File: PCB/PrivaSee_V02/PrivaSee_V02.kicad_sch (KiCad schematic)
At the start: 22 parts, among them J2 Batt_Solder_Point, SW1 (Generic toggle state switch), U2 LM358, U3 254, U4 DFR0568, U5 LM358, U6 ESP32-C5-DevKitC-1

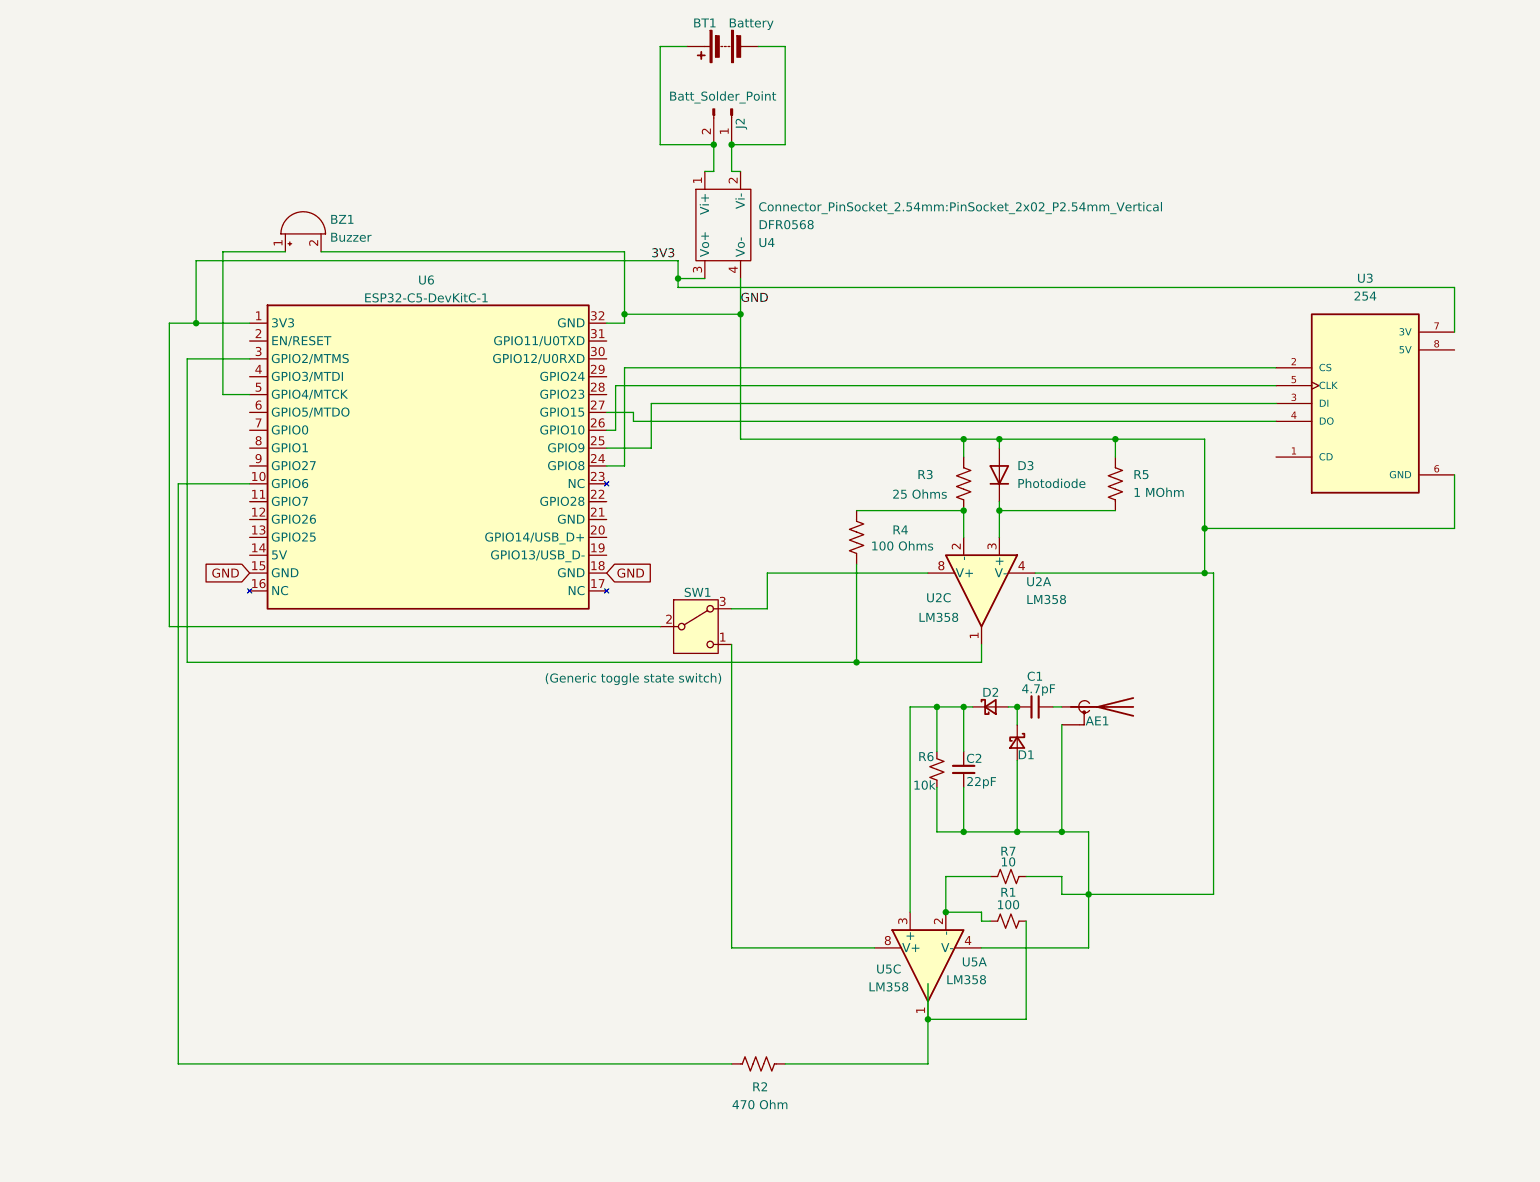
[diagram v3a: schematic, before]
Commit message: PCB Updates
Added a screen, updated the connector for the SMA through hole component, and rearranged to fit
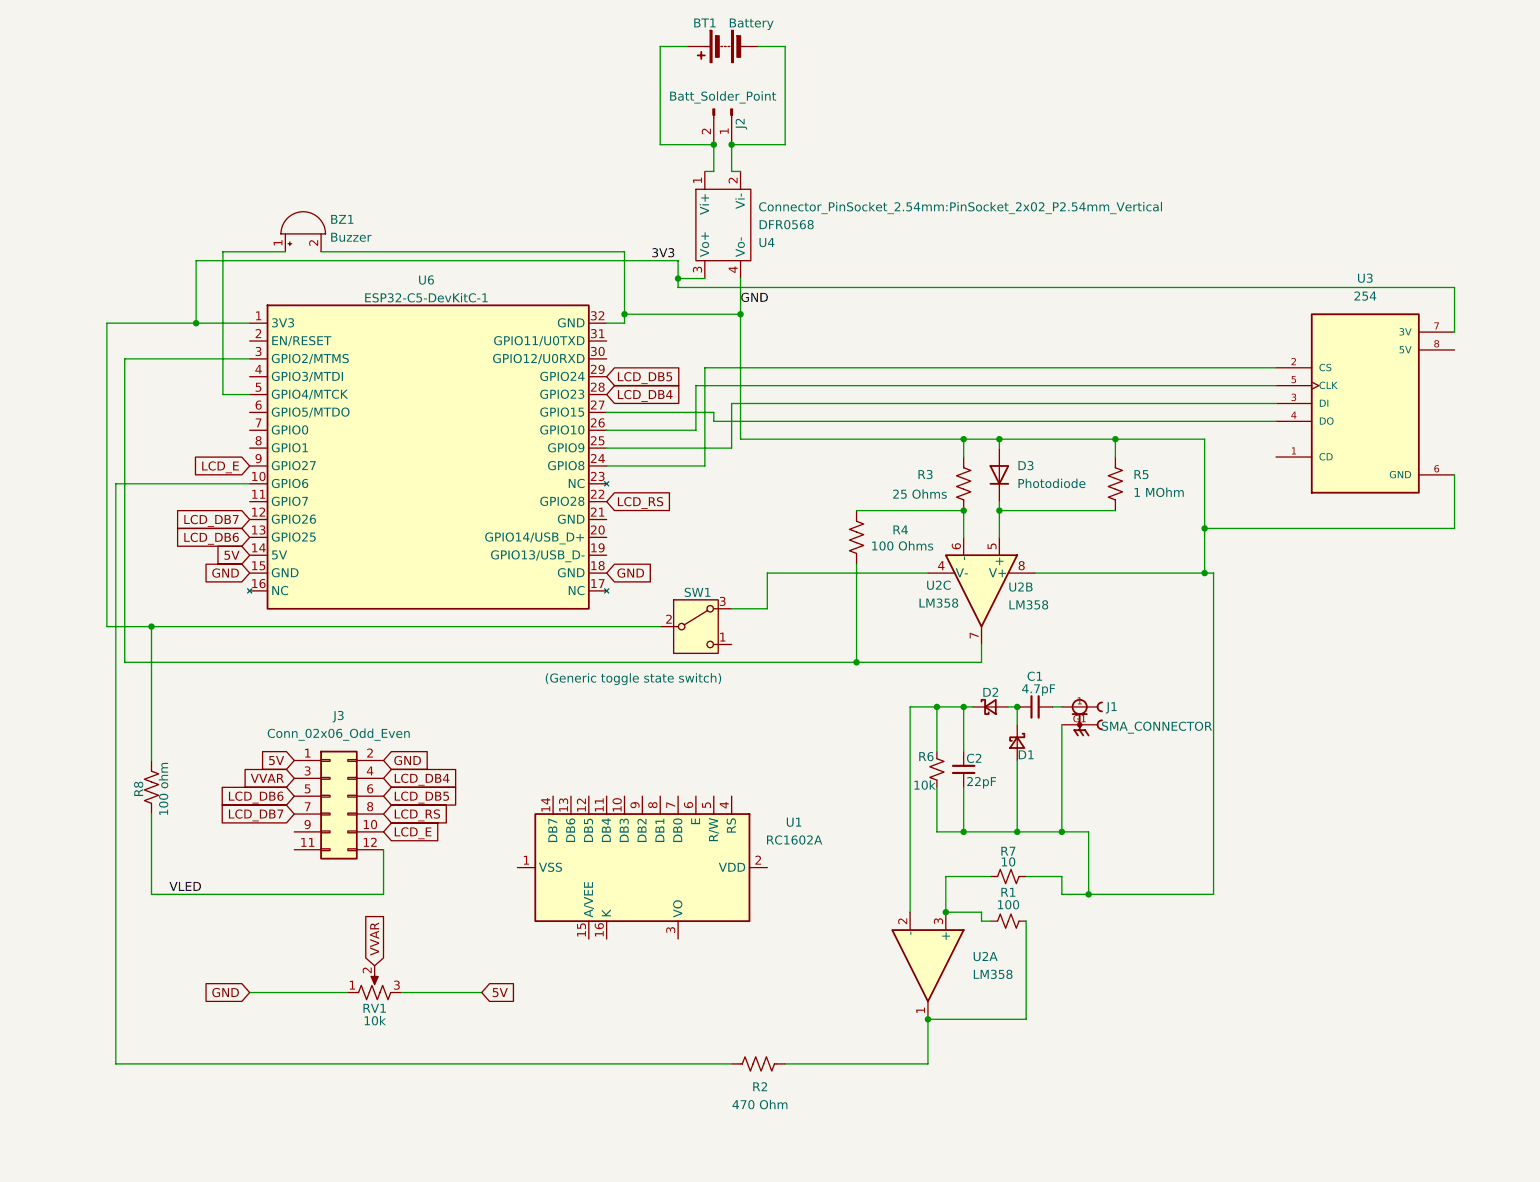
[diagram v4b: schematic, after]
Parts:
- removed AE1: SMA_Conn, RF_Antenna:Johanson_2450AT18x100_2400-2500Mhz, symbol Device:Antenna_Shield
- removed U5: LM358, Package_DIP:DIP-8_W7.62mm, symbol Amplifier_Operational:LM358
- added J1: SMA_CONNECTOR, SMA_CONNECTOR:LPRS_SMA_CONNECTOR, symbol SMA_CONNECTOR:SMA_CONNECTOR
- added J3: Conn_02x06_Odd_Even, Connector_PinHeader_2.54mm:PinHeader_2x06_P2.54mm_Vertical, symbol Connector_Generic:Conn_02x06_Odd_Even
- added R8: 100 ohm, Resistor_SMD:R_1206_3216Metric_Pad1.30x1.75mm_HandSolder, symbol Device:R_US
- added RV1: 10k, Potentiometer_THT:Potentiometer_ACP_CA6-H2,5_Horizontal, symbol Device:R_Potentiometer_US
- added U1: RC1602A, Display:RC1602A, symbol Display_Character:RC1602A
- added unit 2 of U2
- U2: footprint Package_DIP:DIP-8_W7.62mm -> Package_DIP:DIP-8_W7.62mm_Socket
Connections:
- net 3V3: now also R8.1
- net GND: now also U2.8 (V+), J1.G1, J1.G2, J1.G3, J1.G4, J3.2 (Pin_2), RV1.1; no longer U2.4 (V-)
- net at R4.2, U6.3 (GPIO2/MTMS): now also U2.7; no longer U2.1
- net at R3.2, R4.1: now also U2.6 (-); no longer U2.2 (-)
- net at D3.1 (K), R5.2: now also U2.5 (+); no longer U2.3 (+)
- net at R1.2, R2.2: now also U2.1
- net at R1.1, R7.1: now also U2.3 (+)
- net at C2.2, D2.1 (K), R6.1: now also U2.2 (-)
- net at C1.2: now also J1.1
- net LCD_DB7: now reaches U6.12 (GPIO26)
- net LCD_DB7: now also J3.7 (Pin_7)
- net LCD_DB6: now reaches U6.13 (GPIO25)
- net LCD_DB6: now also J3.5 (Pin_5)
- net 5V: now reaches U6.14 (5V)
- net 5V: now also J3.1 (Pin_1), RV1.3
- net LCD_RS: now reaches U6.22 (GPIO28)
- net LCD_RS: now also J3.8 (Pin_8)
- net LCD_DB4: now reaches U6.28 (GPIO23)
- net LCD_DB4: now also J3.4 (Pin_4)
- net LCD_DB5: now reaches U6.29 (GPIO24)
- net LCD_DB5: now also J3.6 (Pin_6)
- net LCD_E: now reaches U6.9 (GPIO27)
- net LCD_E: now also J3.10 (Pin_10)
- net at SW1.3 (A): now also U2.4 (V-); no longer U2.8 (V+)
- new net VLED: J3.12 (Pin_12), R8.2
- new net VVAR: J3.3 (Pin_3), RV1.2

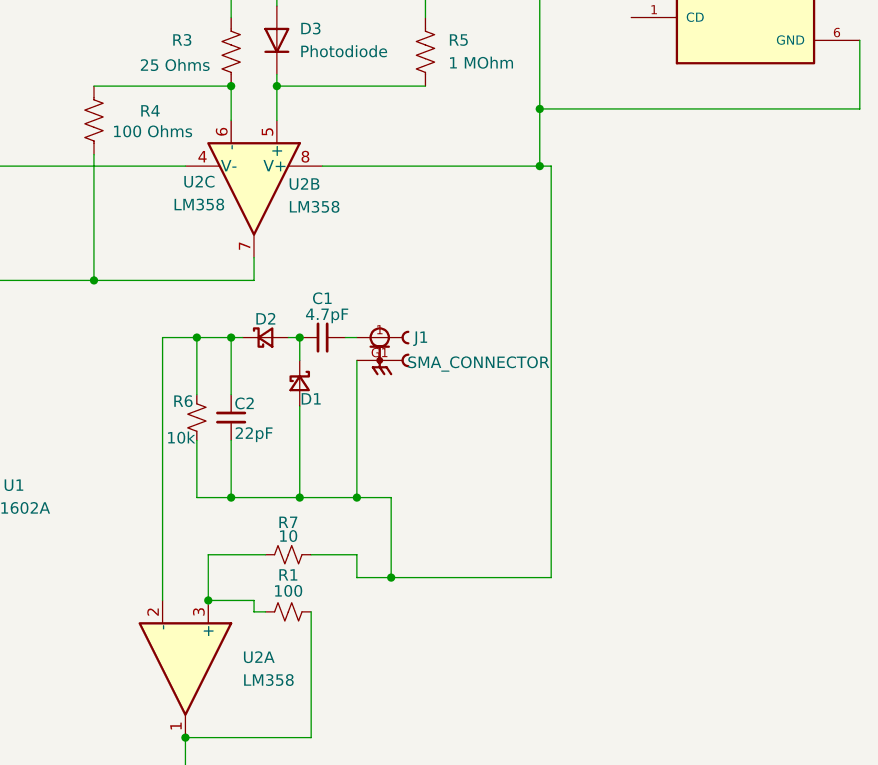
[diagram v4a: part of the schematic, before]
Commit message: RF parts placed
Swapped out the schematic with my components
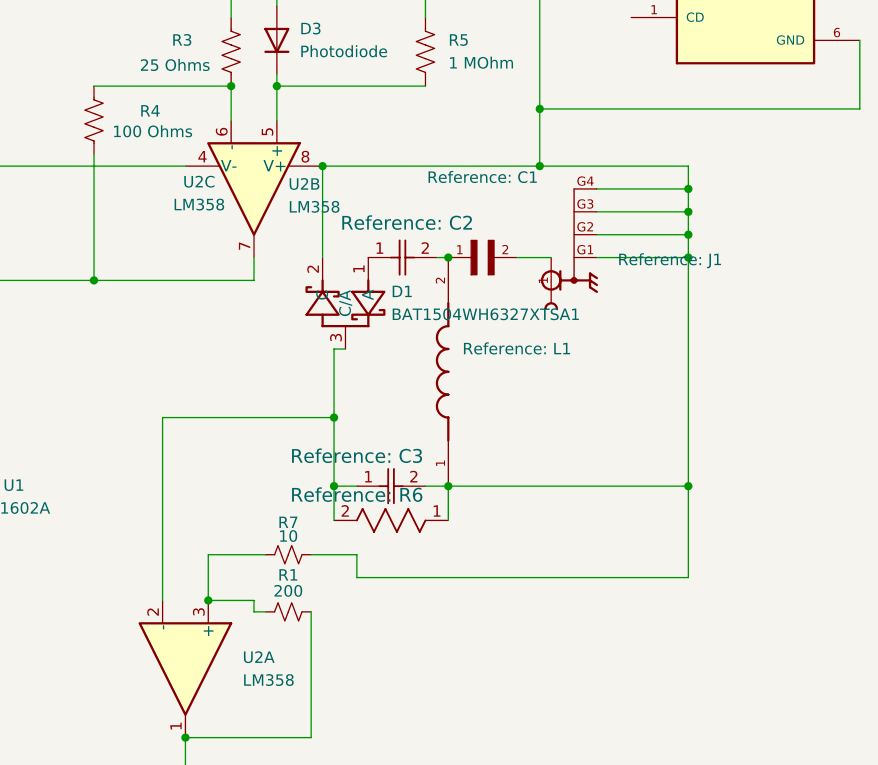
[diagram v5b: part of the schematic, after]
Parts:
- removed C1: 4.7pF, Capacitor_SMD:C_0402_1005Metric_Pad0.74x0.62mm_HandSolder, symbol Device:C_Small
- removed C2: 22pF, Capacitor_SMD:C_0402_1005Metric_Pad0.74x0.62mm_HandSolder, symbol Device:C_Small
- removed D1, D2: Schottky, Diode_SMD:D_0402_1005Metric_Pad0.77x0.64mm_HandSolder, symbol Device:D_Schottky_Small
- removed J1: SMA_CONNECTOR, SMA_CONNECTOR:LPRS_SMA_CONNECTOR, symbol SMA_CONNECTOR:SMA_CONNECTOR
- removed R6: 10k, Resistor_SMD:R_0402_1005Metric_Pad0.72x0.64mm_HandSolder, symbol Device:R_Small_US
- added C1: GJM1555C1HR22BB01D, Snapeda:CAPC1005X55N, symbol Snapeda:GJM1555C1HR22BB01D
- added C2: GJM1555C1H4R7CB01D, Snapeda:G-155_MUR-L, symbol Snapeda:GJM1555C1H4R7CB01D
- added C3: GJM1555C1H220FB01D, Snapeda:CAP_GJM1555C1H220FB01D_MUR-L, symbol Snapeda:GJM1555C1H220FB01D
- added D1: BAT1504WH6327XTSA1, JLCImport:BAT1504WH6327XTSA1, symbol JLCImport:BAT1504WH6327XTSA1
- added J1: RFPC-SMA27-F, Snapeda:GRADCONN_RFPC-SMA27-F, symbol Snapeda:RFPC-SMA27-F
- added L1: LQP02HQ9N1H02E, Snapeda:IND_LQP02HQ9N1H02E, symbol Snapeda:LQP02HQ9N1H02E
- added R6: RT0402BRE07100KL, Snapeda:RC0402N_YAG-L, symbol Snapeda:RT0402BRE07100KL
- R1: value 100 -> 200
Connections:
- net GND: now also C3.2, D1.2 (C), J1.G1, J1.G2, J1.G3, J1.G4, L1.1, R6.1
- net at U2.2 (-): now also C3.1, D1.3 (C/A), R6.2
- new net: C2.1, D1.1 (A)
- new net: C1.2, J1.1
- new net: C1.1, C2.2, L1.2

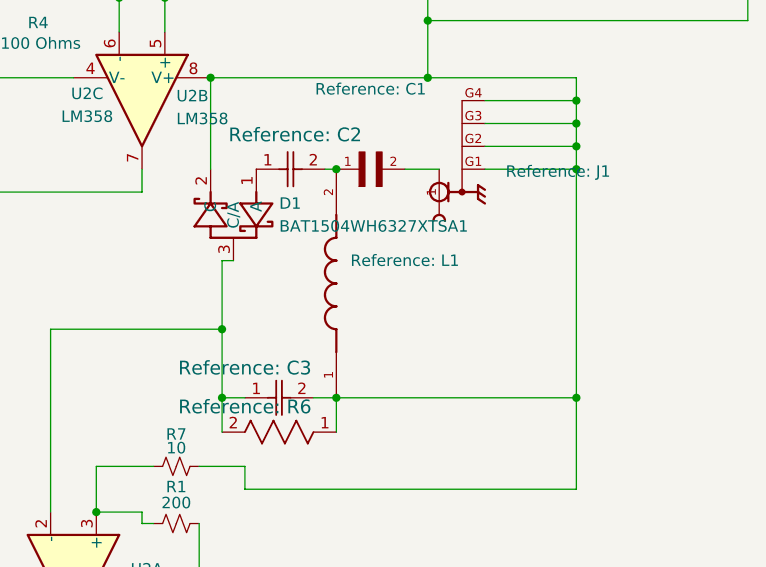
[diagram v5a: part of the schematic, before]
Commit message: CPGW Fencing and Zones
Created area where .2mm for CPGW trace and added vias bordering
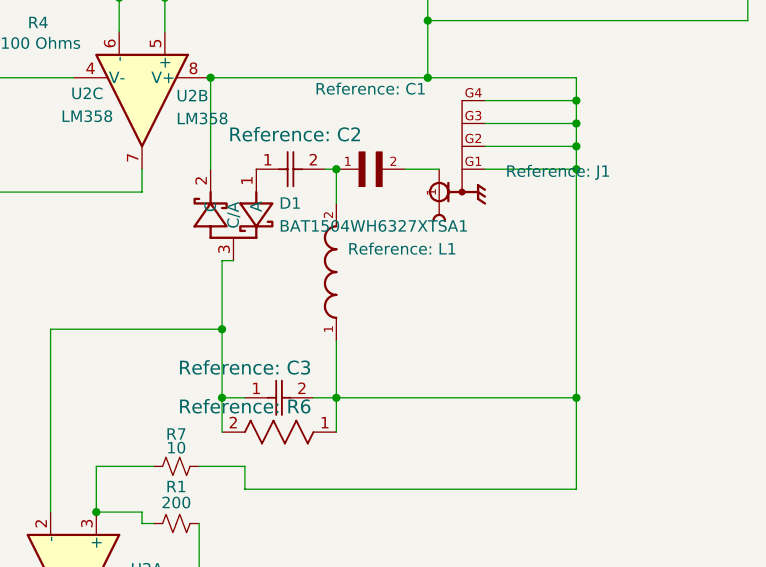
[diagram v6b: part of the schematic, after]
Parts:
- removed L1: LQP02HQ9N1H02E, Snapeda:IND_LQP02HQ9N1H02E, symbol Snapeda:LQP02HQ9N1H02E
- added L1: LQW15AN9N1H00D, Snapeda:INDC1006X60N, symbol Snapeda:LQW15AN9N1H00D
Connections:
- net GND: now also L1.1
- net at C1.1, C2.2: now also L1.2
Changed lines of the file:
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@@
 	)
 	(junction
-		(at 190.5 102.87)
+		(at 217.17 97.79)
 		(diameter 0)
 		(color 0 0 0 0)
 	)
 	(junction
-		(at 217.17 97.79)
+		(at 176.53 92.71)
 		(diameter 0)
 		(color 0 0 0 0)
 	)
 	(junction
-		(at 176.53 92.71)
+		(at 125.73 50.8)
 		(diameter 0)
 		(color 0 0 0 0)
 	)
 	(junction
-		(at 125.73 50.8)
+		(at 190.5 102.87)
 		(diameter 0)
 		(color 0 0 0 0)
@@
 	(wire
 		(pts
+			(xy 190.5 102.87) (xy 190.5 106.68)
+		)
+		(stroke
+			(width 0)
+			(type default)
+		)
+	)
+	(wire
+		(pts
 			(xy 129.54 63.5) (xy 210.82 63.5)
 		)
@@
 	(wire
 		(pts
+			(xy 190.5 121.92) (xy 190.5 128.27)
+		)
+		(stroke
+			(width 0)
+			(type default)
+		)
+	)
+	(wire
+		(pts
 			(xy 129.54 77.47) (xy 115.57 77.47)
 		)
@@
 	)
 	(symbol
-		(lib_id "Snapeda:LQP02HQ9N1H02E")
-		(at 190.5 115.57 90)
-		(unit 1)
-		(body_style 1)
-		(exclude_from_sim no)
-		(in_bom yes)
-		(on_board yes)
-		(in_pos_files yes)
-		(dnp no)
-		(property "Reference" "L1"
-			(at 198.12 113.03 90)
-			(show_name yes)
-			(do_not_autoplace no)
-			(effects
-				(font
-					(size 1.27 1.27)
-				)
-			)
-		)
-		(property "Value" "LQP02HQ9N1H02E"
-			(at 198.882 116.332 90)
-			(hide yes)
-			(show_name yes)
-			(do_not_autoplace no)
-			(effects
-				(font
-					(size 1.27 1.27)
-				)
-			)
-		)
-		(property "Footprint" "Snapeda:IND_LQP02HQ9N1H02E"
-			(at 184.15 115.57 0)
-			(hide yes)
-			(show_name yes)
-			(do_not_autoplace no)
-			(effects
-				(font
-					(size 1.27 1.27)
-				)
-			)
-		)
-		(property "Datasheet" ""
-			(at 190.5 115.57 0)
-			(hide yes)
-			(show_name yes)
-			(do_not_autoplace no)
-			(effects
-				(font
-					(size 1.27 1.27)
-				)
-			)
-		)
-		(property "Description" ""
-			(at 190.5 115.57 0)
-			(hide yes)
-			(show_name yes)
-			(do_not_autoplace no)
-			(effects
-				(font
-					(size 1.27 1.27)
-				)
-			)
-		)
-		(property "PARTREV" "L1"
-			(at 186.69 115.57 0)
-			(hide yes)
-			(show_name yes)
-			(do_not_autoplace no)
-			(effects
-				(font
-					(size 1.27 1.27)
-				)
-			)
-		)
-		(property "STANDARD" "Manufacturer Recommendations"
-			(at 181.61 115.57 0)
-			(hide yes)
-			(show_name yes)
-			(do_not_autoplace no)
-			(effects
-				(font
-					(size 1.27 1.27)
-				)
-			)
-		)
-		(property "MAXIMUM_PACKAGE_HEIGHT" "0.32 mm"
-			(at 184.15 115.57 0)
-			(hide yes)
-			(show_name yes)
-			(do_not_autoplace no)
-			(effects
-				(font
-					(size 1.27 1.27)
-				)
-			)
-		)
-		(property "MANUFACTURER" "Murata"
-			(at 186.69 115.57 0)
-			(hide yes)
-			(show_name yes)
-			(do_not_autoplace no)
-			(effects
-				(font
-					(size 1.27 1.27)
-				)
-			)
-		)
-		(pin "2"
-		)
-		(pin "1"
-		)
-		(instances
-			(project "PrivaSee_V02"
-				(path "/e2eea558-d7b1-4123-919c-3783d093c9eb"
-					(reference "L1")
-					(unit 1)
-				)
-			)
-		)
-	)
-	(symbol
 		(lib_id "Display_Character:RC1602A")
 		(at 120.65 134.62 270)
@@
 					(unit 1)
 				)
+			)
+		)
+	)
+	(symbol
+		(lib_id "Snapeda:LQW15AN9N1H00D")
+		(at 190.5 114.3 90)
+		(unit 1)
+		(body_style 1)
+		(exclude_from_sim no)
+		(in_bom yes)
+		(on_board yes)
+		(in_pos_files yes)
+		(dnp no)
+		(fields_autoplaced yes)
+		(property "Reference" "L1"
+			(at 191.77 111.7599 90)
+			(show_name yes)
+			(do_not_autoplace no)
+			(effects
+				(font
+					(size 1.27 1.27)
+				)
+				(justify right)
+			)
+		)
+		(property "Value" "LQW15AN9N1H00D"
+			(at 191.77 114.2999 90)
+			(hide yes)
+			(show_name yes)
+			(do_not_autoplace no)
+			(effects
+				(font
+					(size 1.27 1.27)
+				)
+				(justify right)
+			)
+		)
+		(property "Footprint" "Snapeda:INDC1006X60N"
+			(at 191.77 116.8399 90)
+			(hide yes)
+			(show_name yes)
+			(do_not_autoplace no)
+			(effects
+				(font
+					(size 1.27 1.27)
+				)
+				(justify right)
+			)
+		)
+		(property "Datasheet" ""
+			(at 190.5 114.3 0)
+			(hide yes)
+			(show_name yes)
+			(do_not_autoplace no)
+			(effects
+				(font
+					(size 1.27 1.27)
+				)
+			)
+		)
+		(property "Description" ""
+			(at 190.5 114.3 0)
+			(hide yes)
+			(show_name yes)
+			(do_not_autoplace no)
+			(effects
+				(font
+					(size 1.27 1.27)
+				)
+			)
+		)
+		(pin "1"
+		)
+		(pin "2"
+		)
+		(instances
+			(project "PrivaSee_V02"
+				(path "/e2eea558-d7b1-4123-919c-3783d093c9eb"
+					(reference "L1")
+					(unit 1)
+				)
